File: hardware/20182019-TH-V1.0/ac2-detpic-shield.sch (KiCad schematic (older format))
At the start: 45 parts, among them J1 HEADER, J2 HEADER, J3 HEADER, J4 HEADER, J5 HEADER, J6 HEADER, J7 HEADER, Q1 VN2222, Q2 VN2222, SW1 SW_DIP_x04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

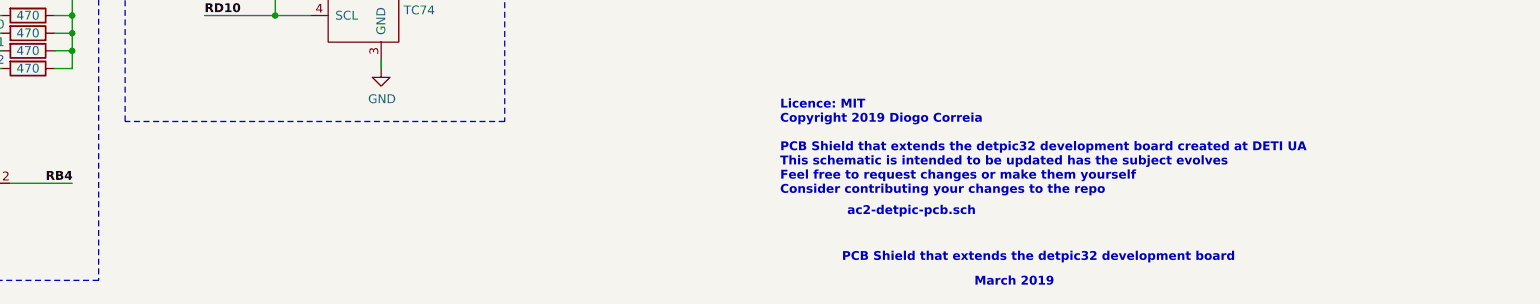
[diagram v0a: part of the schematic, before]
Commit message: added gnd test point to 20182019-TH v1.1
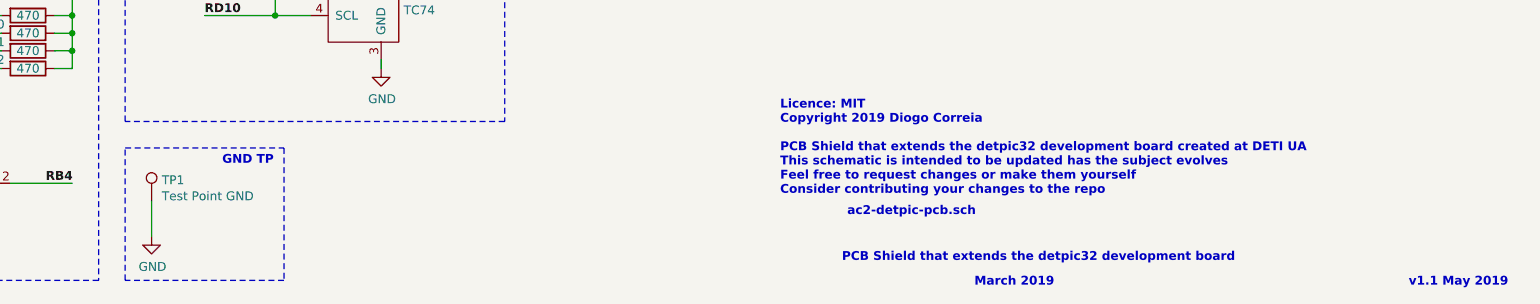
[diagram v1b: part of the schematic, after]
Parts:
- added TP1: Test Point GND, TestPoint:TestPoint_Pad_2.5x2.5mm, symbol Connector:TestPoint
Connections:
- wire segments 171 -> 172
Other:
- note added: "GND TP"
- note added: "v1.1 May 2019"
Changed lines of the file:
@@
 Wire Wire Line
 	2700 3550 2600 3550
+$Comp
+L Connector:TestPoint TP1
+U 1 1 5CE0C159
+P 3450 7150
+F 0 "TP1" H 3508 7268 50  0000 L CNN
+F 1 "Test Point GND" H 3508 7177 50  0000 L CNN
+F 2 "TestPoint:TestPoint_Pad_2.5x2.5mm" H 3650 7150 50  0001 C CNN
+F 3 "~" H 3650 7150 50  0001 C CNN
+	1    3450 7150
+	1    0    0    -1
+$EndComp
+$Comp
+L power:GND #PWR04
+U 1 1 5CE0CF54
+P 3450 7350
+F 0 "#PWR04" H 3450 7100 50  0001 C CNN
+F 1 "GND" H 3455 7177 50  0000 C CNN
+F 2 "" H 3450 7350 50  0001 C CNN
+F 3 "" H 3450 7350 50  0001 C CNN
+	1    3450 7350
+	1    0    0    -1
+$EndComp
+Wire Wire Line
+	3450 7150 3450 7350
+Wire Notes Line
+	3300 6850 4200 6850
+Wire Notes Line
+	4200 6850 4200 7600
+Wire Notes Line
+	4200 7600 3300 7600
+Wire Notes Line
+	3300 7600 3300 6850
+Text Notes 3850 6950 0    50   ~ 10
+GND TP
+Text Notes 10570 7640 0    50   ~ 10
+v1.1 May 2019
 $EndSCHEMATC
